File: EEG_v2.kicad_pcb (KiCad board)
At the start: 2 copper layers, 113 parts, among them P1 CONN_2, P2 CONN_8, P3 USB-MINI-B, P4 CONN_8, P5 CONN_5X2, P6 CONN_3, SW1 SWITCH_INV, SW2 RESET, SW3 SW_PUSH, SW4 SW_PUSH, U1 ADS1299IPAGR, U2 TLV70033, U3 TLV70025, U4 LM2664, U5 TPS72325, U6 CC2540, U7 2450BM15A0002E, X1 QUARTZCMS4_32K, X2 32-MHz

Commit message: Continued layout work.
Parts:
- C10, C14, C15, C23, C24, C27, C28, C29, C30, C31, C32, C33, C4, C5, C6, C9: footprint c_0603 -> Murata_GRM_0603
- R10, R11, R12, R13, R14, R15, R16, R17, R18, R19, R2, R20, R3, R4, R5, R6, R7, R8: footprint SM0603_Resistor -> Vishay_CRCW_0603
- moved C22 82.5 mm to (320.5, 158.0), turned to 180 degrees
- moved C9 79.3 mm to (321.7, 172.1), turned to 270 degrees
- moved C10 79.0 mm to (318.3, 172.1), turned to 270 degrees
- moved R11 75.5 mm to (315.0, 172.1), turned to 270 degrees
- moved TP3 74.8 mm to (323.1, 144.9)
- moved R7 68.2 mm to (319.4, 172.1), turned to 270 degrees
- moved R2 67.8 mm to (329.4, 172.1), turned to 270 degrees
- moved C4 67.1 mm to (327.2, 172.1), turned to 270 degrees
- moved R6 66.3 mm to (320.5, 172.1), turned to 270 degrees
- moved P2 64.6 mm to (323.5, 177.3), turned to 180 degrees
- moved R16 63.8 mm to (306.1, 172.1), turned to 270 degrees
- moved R3 63.7 mm to (328.3, 172.1), turned to 270 degrees
- moved C5 63.1 mm to (326.1, 172.1), turned to 270 degrees
- moved R14 61.9 mm to (307.2, 172.1), turned to 270 degrees
- moved TP2 61.8 mm to (306.1, 136.0)
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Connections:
- net N-00000102 renamed /Power/N3.3V
- C10 pad 1: AGND -> N-0000072
- C10 pad 2: N-0000072 -> AGND
- C15 pad 1: AGND -> N-0000097
- C15 pad 2: N-0000097 -> AGND
- C24 pad 1: AGND -> N-0000095
- C24 pad 2: N-0000094 (its old number) -> AGND
- C28 pad 1: AGND -> N-0000090
- C28 pad 2: N-0000090 -> AGND
- C31 pad 1: AGND -> N-0000089
- C31 pad 2: N-0000089 -> AGND
- C33 pad 1: AGND -> N-0000092
- C33 pad 2: N-0000092 -> AGND
- C4 pad 1: AGND -> N-0000079
- C4 pad 2: N-0000080 -> AGND
- C6 pad 1: AGND -> N-0000070
- C6 pad 2: N-0000070 -> AGND
- R13 pad 1: N-0000094 (its old number) -> N-0000095
- R3 pad 1: N-0000080 -> N-0000079
- U1 pad 15: N-0000080 -> N-0000079
- U1 pad 7: N-0000094 (its old number) -> N-0000095

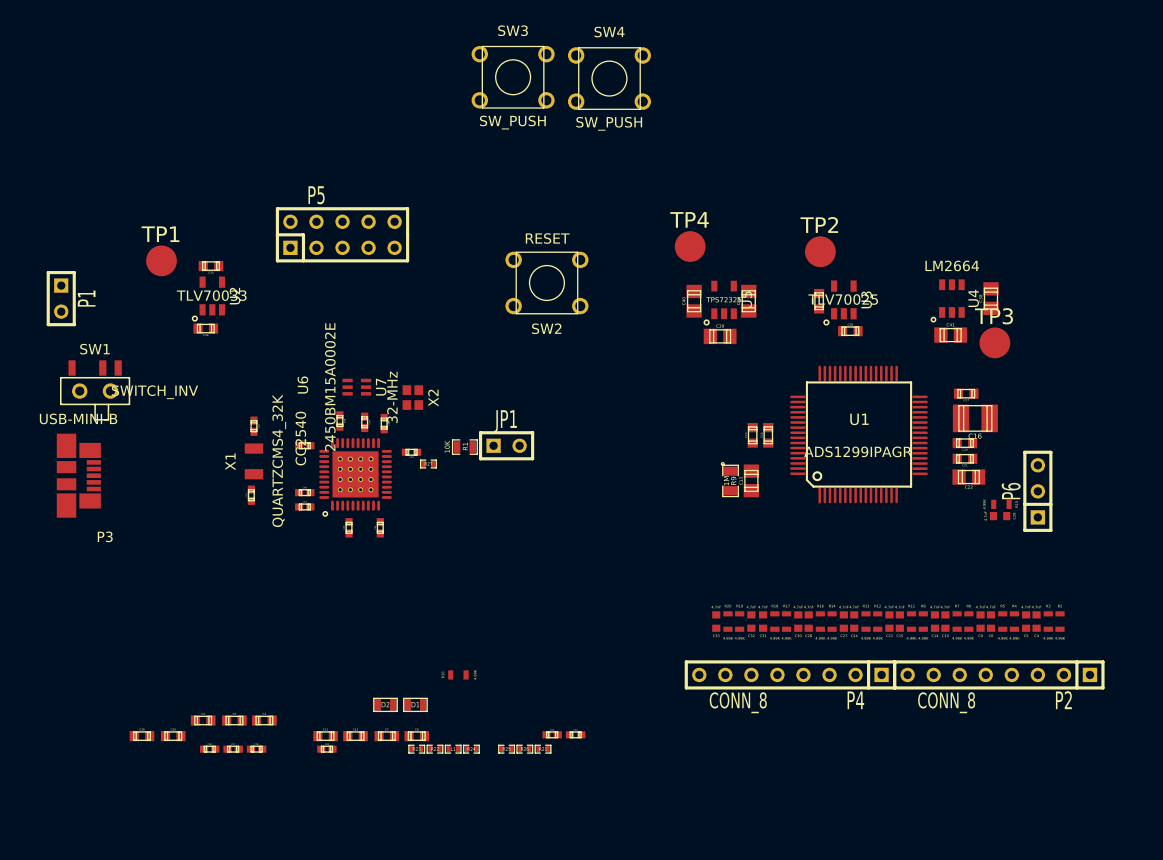
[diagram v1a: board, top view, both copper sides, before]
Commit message: Change USB connector. Continue layout.
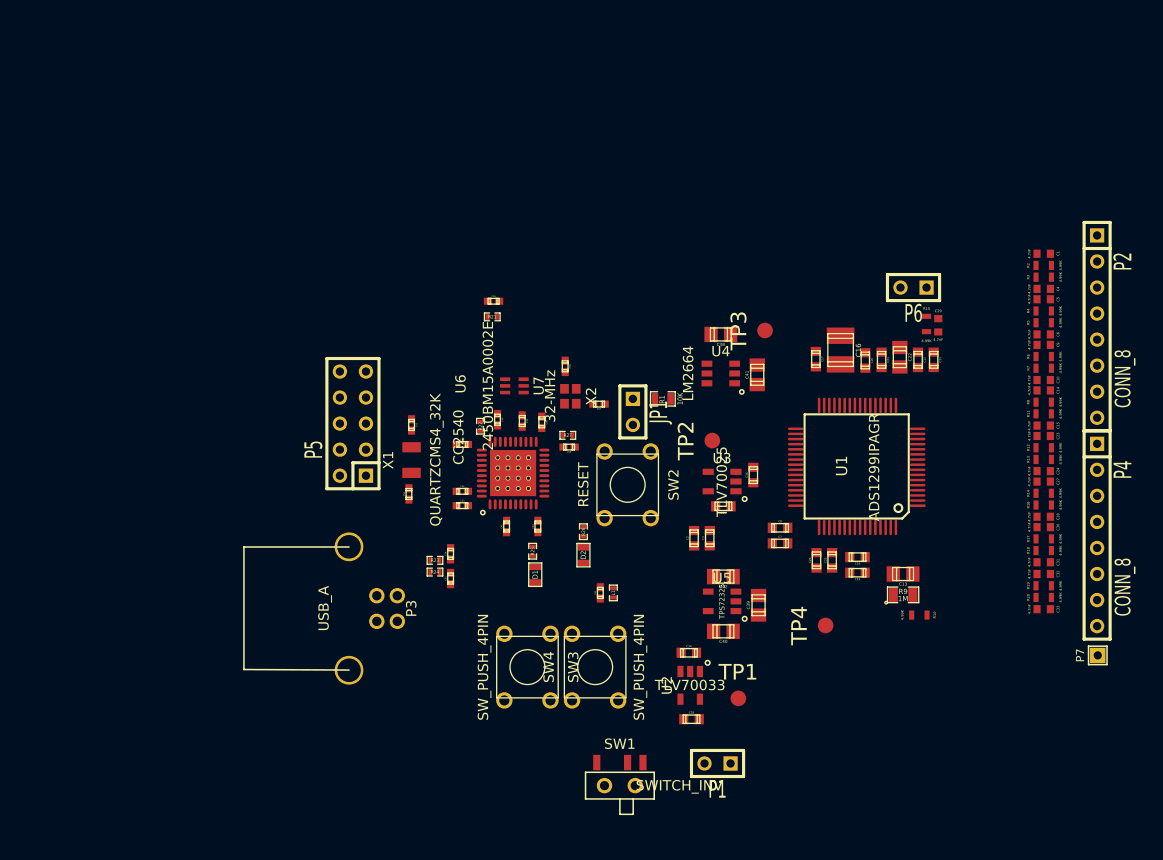
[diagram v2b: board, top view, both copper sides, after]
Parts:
- added P7: CONN_1, SIL-1, F.Cu at (333.1, 175.4)
- C1: footprint c_0603 -> Murata_GRM_0603
- P3: value USB-MINI-B -> USB_A; footprint 47346-0001 -> 61729-0010BLF
- P6: value CONN_3 -> CONN_2; footprint SIL-3 -> SIL-2
- SW3, SW4: value SW_PUSH -> SW_PUSH_4PIN
- TP1, TP2, TP3, TP4: footprint Measurement_Point_Round-SMD-Pad_Big -> Measurement_Point_Round-SMD-Pad_Small
- moved C1 88.6 mm to (327.9, 136.2)
- moved P1 78.4 mm to (296.0, 185.9), turned to 180 degrees
- moved TP1 70.6 mm to (298.1, 179.6)
- moved C11 69.7 mm to (317.1, 146.6), turned to 270 degrees
- moved C26 68.0 mm to (305.7, 166.1), turned to 90 degrees
- moved C25 66.5 mm to (307.2, 166.1), turned to 90 degrees
- moved C12 66.0 mm to (315.6, 146.6), turned to 270 degrees
- moved C35 64.4 mm to (293.5, 181.6), turned to 0 degrees
- moved SW1 64.0 mm to (286.5, 188.1)
- moved U2 60.1 mm to (293.4, 178.3), turned to 180 degrees
- moved SW3 57.5 mm to (277.5, 176.5), turned to 270 degrees
- moved SW4 57.4 mm to (284.1, 176.5), turned to 90 degrees
- moved C34 56.7 mm to (293.2, 175.1), turned to 0 degrees
- moved C2 51.1 mm to (293.8, 164.0), turned to 90 degrees
- moved C58 51.0 mm to (281.2, 147.2), turned to 270 degrees
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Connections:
- net N-0000033 renamed /VBUS
- P3 pad 4: (no net) -> AGND
- SW2 pad 2: /Microcontroller/RESET_N -> AGND
- SW2 pad 3: (no net) -> /Microcontroller/RESET_N
- SW2 pad 4: (no net) -> /Microcontroller/RESET_N
- SW3 pad 2: N-0000058 (its old number) -> AGND
- SW3 pad 3: (no net) -> N-0000060
- SW3 pad 4: (no net) -> N-0000060
- SW4 pad 2: N-0000054 (its old number) -> AGND
- SW4 pad 3: (no net) -> N-0000050
- SW4 pad 4: (no net) -> N-0000050
- U6 pad 13: /Analog Frontend/CS -> /Analog Frontend/DRDY
- U6 pad 14: /Microcontroller/SCK -> /Analog Frontend/DOUT
- U6 pad 15: (no net) -> /Analog Frontend/DIN
- U6 pad 16: /Analog Frontend/DIN -> /Microcontroller/SCK
- U6 pad 17: /Analog Frontend/DOUT -> (no net)
- U6 pad 18: /Analog Frontend/DRDY -> /Analog Frontend/CS
- U6 pad 7: N-0000058 (its old number) -> N-0000060
- U6 pad 8: N-0000054 (its old number) -> N-0000050

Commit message: Change layout.
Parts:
- moved P6 4.64 mm to (319.8, 139.7)
- moved R15 4.27 mm to (320.7, 143.4)
- moved C29 4.13 mm to (321.7, 143.4)
- moved JP1 0.64 mm to (287.8, 151.0)
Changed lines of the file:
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@@
   )
   (module SIL-2 (layer F.Cu)
-    (at 287.782 151.638 270)
+    (at 287.782 151.003 270)
     (descr "Connecteurs 2 pins")
     (tags "CONN DEV")
@@
   )
   (module Vishay_CRCW_0603 (layer F.Cu)
-    (at 316.4205 143.0655 270)
+    (at 320.675 143.383 270)
     (clearance 0.1)
     (fp_text reference R15 (at -1.5 0 360) (layer F.SilkS)
@@
   )
   (module Murata_GRM_0603 (layer F.Cu)
-    (at 317.5635 143.1925 90)
+    (at 321.691 143.383 90)
     (solder_mask_margin 0.07)
     (clearance 0.1)
@@
   )
   (module SIL-2 (layer F.Cu)
-    (at 315.1505 139.5095 180)
+    (at 319.786 139.7 180)
     (descr "Connecteurs 2 pins")
     (tags "CONN DEV")

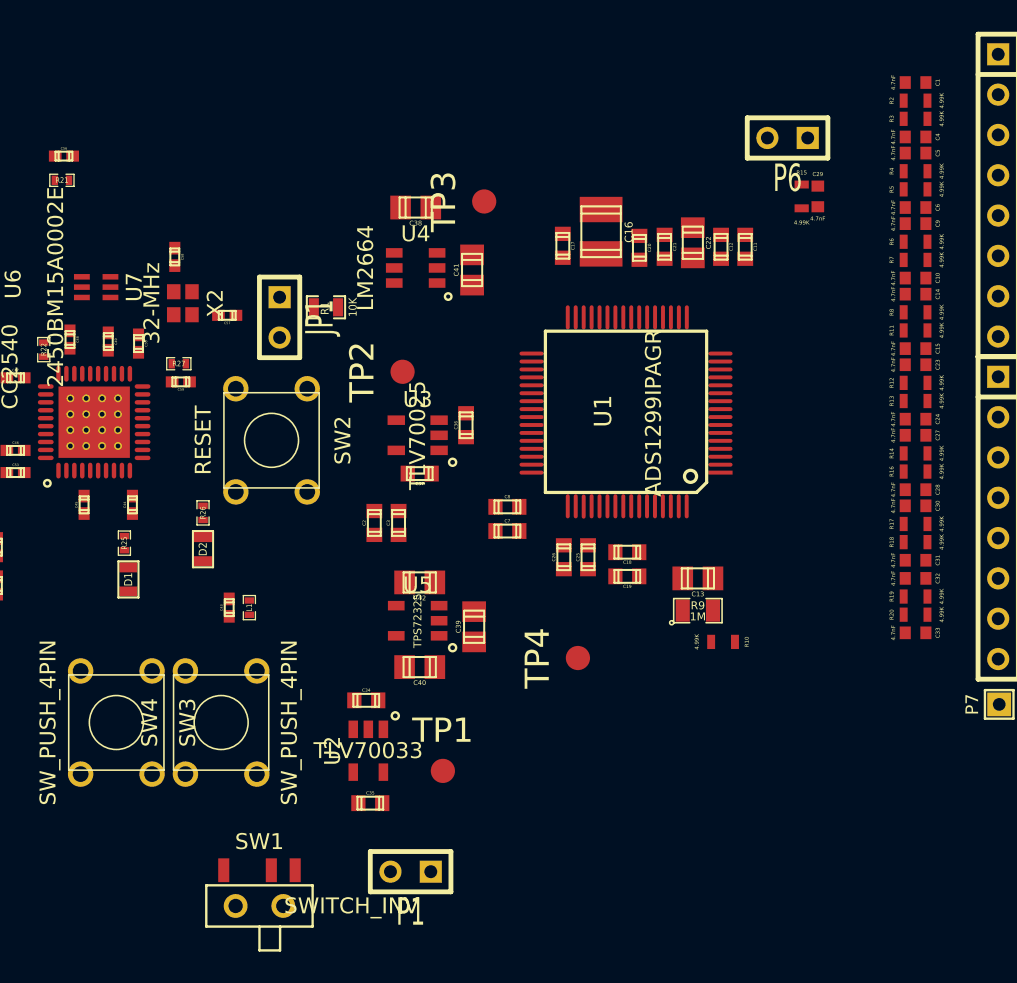
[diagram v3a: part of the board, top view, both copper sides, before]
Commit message: Continue layout on ADS side, power supplies complete.
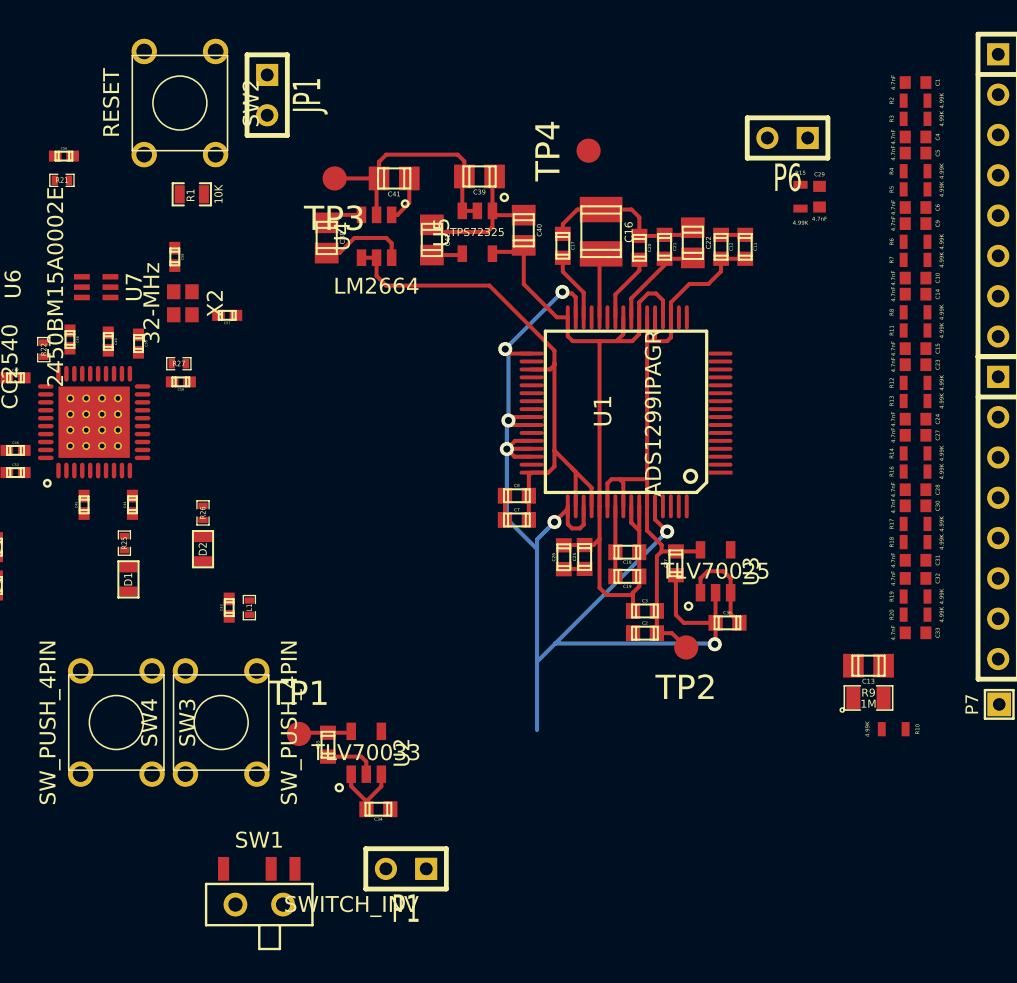
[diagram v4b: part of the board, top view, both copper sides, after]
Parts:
- moved TP4 32.0 mm to (307.2, 140.5)
- moved C39 28.4 mm to (300.4, 142.1), turned to 180 degrees
- moved C40 28.3 mm to (303.2, 145.5), turned to 270 degrees
- moved TP2 24.9 mm to (313.4, 171.8), turned to 180 degrees
- moved U5 24.8 mm to (300.2, 145.6), turned to 180 degrees
- moved SW2 22.0 mm to (281.5, 137.5)
- moved C42 21.6 mm to (297.4, 146.1), turned to 270 degrees
- moved C36 20.6 mm to (316.0, 170.2), turned to 0 degrees
- moved U3 20.6 mm to (315.2, 167.0), turned to 0 degrees
- moved C2 18.4 mm to (310.8, 170.9), turned to 0 degrees
- moved C37 17.1 mm to (312.8, 166.5), turned to 90 degrees
- moved C3 16.5 mm to (310.8, 169.5), turned to 0 degrees
- moved JP1 14.0 mm to (287.0, 137.0)
- moved C13 12.1 mm to (324.9, 172.9)
- moved R10 12.1 mm to (326.5, 176.9)
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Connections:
- net N-0000067 renamed /Analog Frontend/VCAP4
- net N-0000068 renamed /Analog Frontend/BIASINV
- net N-0000083 renamed /Analog Frontend/BIASOUT_IN
- net N-0000084 renamed /Analog Frontend/VCAP3
- net N-0000085 renamed /Analog Frontend/VREFP
- C16 pad 1: N-0000078 (its old number) -> /Analog Frontend/VCAP1
- C17 pad 1: N-0000079 (its old number) -> /Analog Frontend/VCAP2
- U1 pad 28: N-0000078 (its old number) -> /Analog Frontend/VCAP1
- U1 pad 30: N-0000079 (its old number) -> /Analog Frontend/VCAP2
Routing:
- net AGND: track 0.00 -> 101.6 mm, vias 0 -> 7
- net -2.5V: track 0.00 -> 60.5 mm
- net +3.3V: track 0.00 -> 45.4 mm
- net +2.5V: track 0.00 -> 42.7 mm
- net /Power/N3.3V: track 0.00 -> 16.1 mm
- net /Analog Frontend/VREFP: track 0.00 -> 6.36 mm
- net N-00000100: track 0.00 -> 5.53 mm
- net VIN_RAW: track 0.00 -> 5.20 mm
- net /Analog Frontend/VCAP3: track 0.00 -> 4.42 mm
- net /Analog Frontend/VCAP2: track 0.00 -> 4.30 mm
- net /Analog Frontend/VCAP4: track 0.00 -> 4.26 mm
- net /Analog Frontend/VCAP1: track 0.00 -> 4.04 mm
- net N-00000101: track 0.00 -> 2.40 mm
- net N-0000097: track 0.00 -> 1.95 mm
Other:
- net class Comp added: clearance 0.127, trace_width 0.254, via_dia 0.889, via_drill 0.635

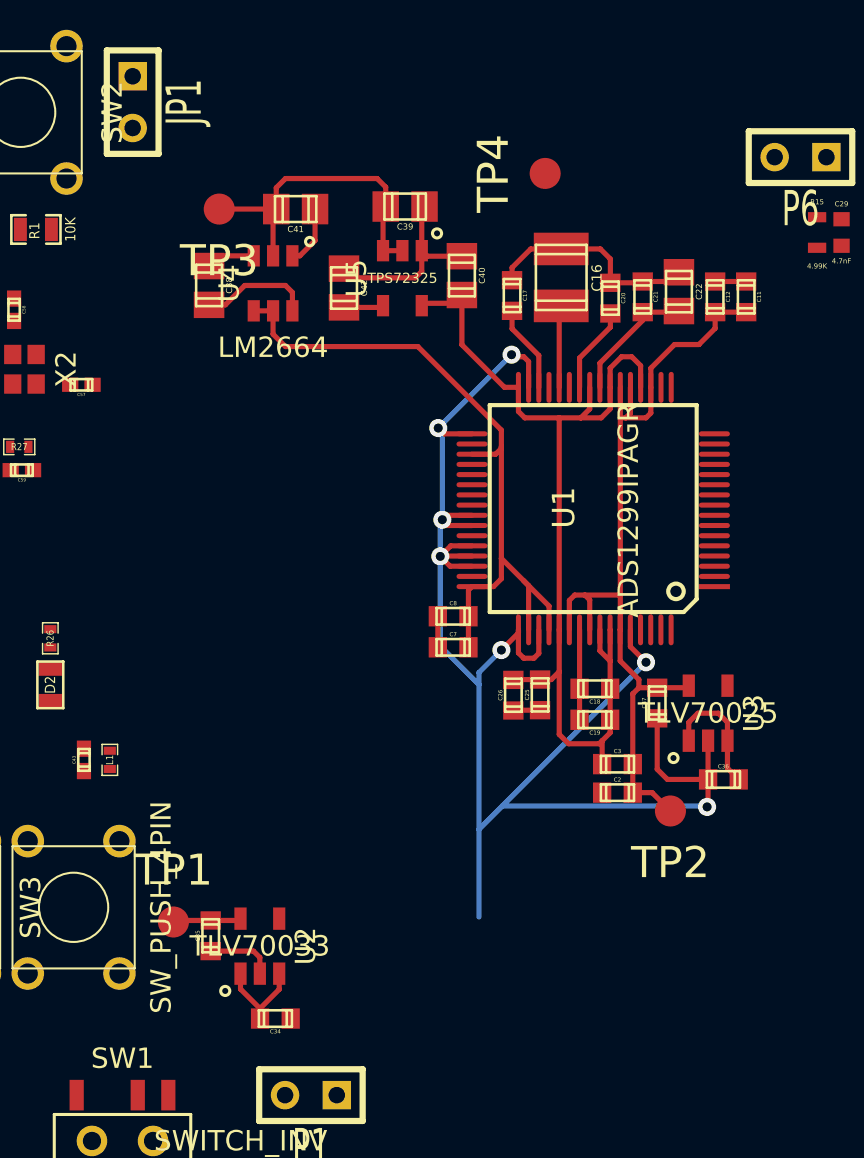
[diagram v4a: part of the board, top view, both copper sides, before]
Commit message: Name nets for convenience on CC2540.
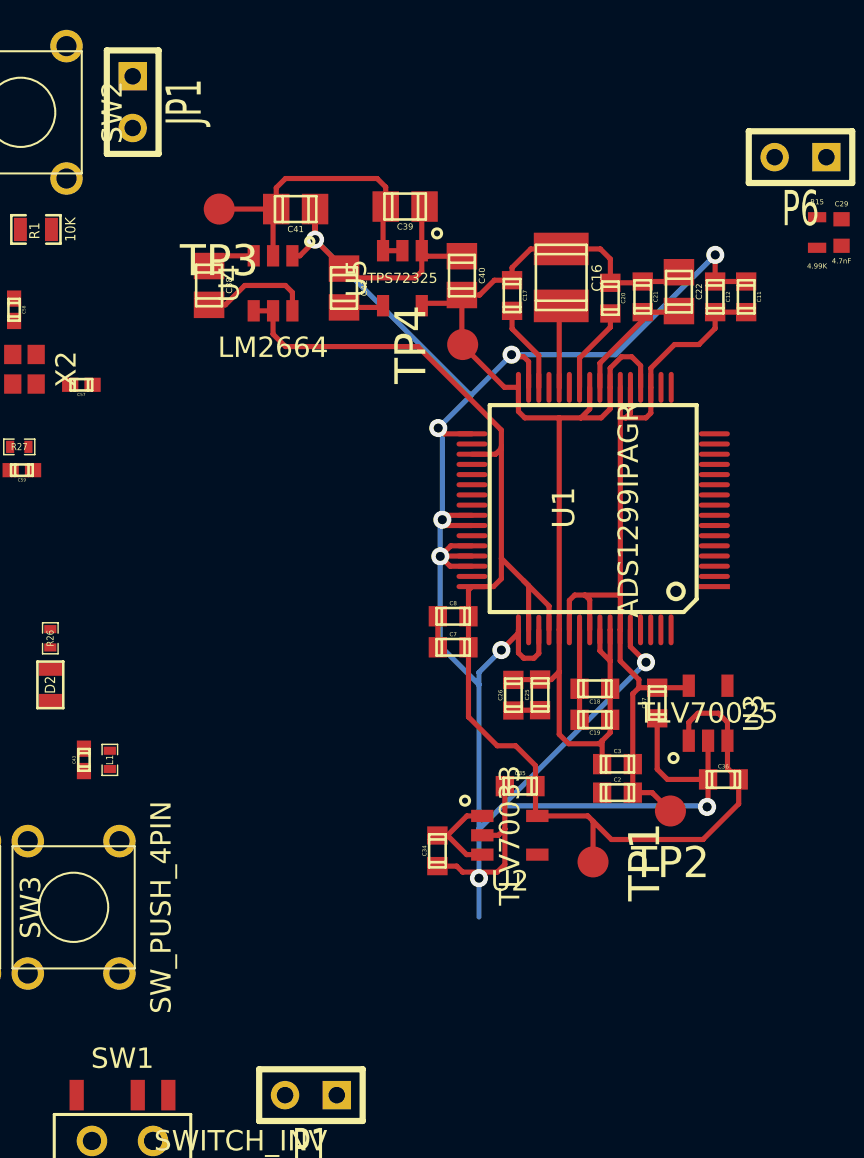
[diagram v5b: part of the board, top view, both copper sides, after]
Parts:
- moved TP1 20.8 mm to (309.6, 174.3), turned to 270 degrees
- moved C35 16.9 mm to (306.0, 170.6), turned to 0 degrees
- moved U2 13.4 mm to (305.5, 173.0), turned to 270 degrees
- moved C34 11.4 mm to (302.0, 173.8), turned to 90 degrees
- moved TP4 9.33 mm to (303.2, 148.9)
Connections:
- net N-0000045 renamed /Microcontroller/RF_P
- net N-0000046 renamed /Microcontroller/RF_N
- net N-0000050 renamed /Microcontroller/SW4
- net N-0000054 renamed /Microcontroller/LED2
- net N-0000055 renamed /Microcontroller/X2_1
- net N-0000056 renamed /Microcontroller/X2_3
- net N-0000057 renamed /Microcontroller/LED1
- net N-0000060 renamed /Microcontroller/SW3
- net N-0000062 renamed /Microcontroller/X1_1
- net N-0000063 renamed /Microcontroller/X1_2
- net N-0000064 renamed /Microcontroller/USB_N_Intr
- net N-0000065 renamed /Microcontroller/USB_P_Intr
- net N-0000066 renamed /Microcontroller/RESET_INTR
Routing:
- net AGND: track 101.6 -> 134.9 mm, vias 7 -> 10
- net +3.3V: track 45.4 -> 66.5 mm
- net -2.5V: track 60.5 -> 63.3 mm
